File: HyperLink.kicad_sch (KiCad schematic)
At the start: 47 parts, among them J1 USB_C_Receptacle_USB2.0, J2 Conn_02x05_Odd_Even, J3 Conn_02x05_Odd_Even, SW1 SW_Push, U1 ESP32-C3, U2 PESD2USB5UXT, U3 MIC5504-3.3YM5, Y1 ABM11W-40.0000MHZ-8-B1U-T3

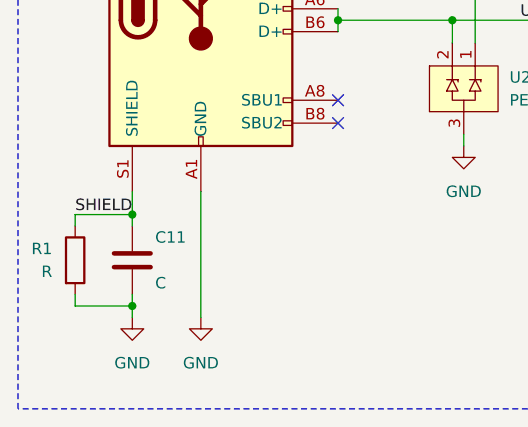
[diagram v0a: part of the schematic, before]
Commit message: Tie SHIELD directly to GND
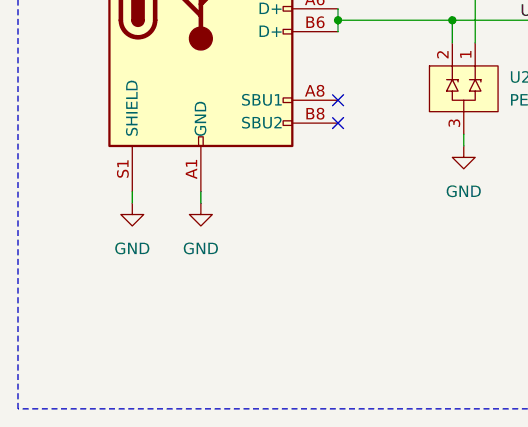
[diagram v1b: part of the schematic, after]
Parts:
- removed C11: C, Capacitor_SMD:C_0402_1005Metric, symbol Device:C
- removed R1: R, Resistor_SMD:R_0402_1005Metric, symbol Device:R
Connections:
- net SHIELD is gone; now on net GND: J1.S1 (SHIELD)
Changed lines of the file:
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@@
   (junction (at 179.07 76.2) (diameter 0) (color 0 0 0 0)
   )
-  (junction (at 29.21 167.64) (diameter 0) (color 0 0 0 0)
-  )
   (junction (at 214.63 139.7) (diameter 0) (color 0 0 0 0)
   )
@@
   )
   (junction (at 250.19 48.26) (diameter 0) (color 0 0 0 0)
-  )
-  (junction (at 29.21 177.8) (diameter 0) (color 0 0 0 0)
   )
   (junction (at 199.39 97.79) (diameter 0) (color 0 0 0 0)
@@
     (stroke (width 0) (type default))
   )
-  (wire (pts (xy 22.86 168.91) (xy 22.86 167.64))
-    (stroke (width 0) (type default))
-  )
   (wire (pts (xy 127 147.32) (xy 119.38 147.32))
     (stroke (width 0) (type default))
@@
     (stroke (width 0) (type default))
   )
-  (wire (pts (xy 29.21 165.1) (xy 29.21 167.64))
-    (stroke (width 0) (type default))
-  )
   (wire (pts (xy 229.87 53.34) (xy 241.3 53.34))
     (stroke (width 0) (type default))
@@
     (stroke (width 0) (type default))
   )
-  (wire (pts (xy 36.83 165.1) (xy 36.83 179.07))
+  (wire (pts (xy 36.83 165.1) (xy 36.83 166.37))
     (stroke (width 0) (type default))
   )
@@
     (stroke (width 0) (type default))
   )
-  (wire (pts (xy 29.21 177.8) (xy 29.21 176.53))
+  (wire (pts (xy 29.21 165.1) (xy 29.21 166.37))
     (stroke (width 0) (type default))
   )
@@
     (stroke (width 0) (type default))
   )
-  (wire (pts (xy 29.21 177.8) (xy 29.21 179.07))
-    (stroke (width 0) (type default))
-  )
   (wire (pts (xy 264.16 48.26) (xy 262.89 48.26))
     (stroke (width 0) (type default))
@@
     (stroke (width 0) (type default))
   )
-  (wire (pts (xy 22.86 177.8) (xy 29.21 177.8))
-    (stroke (width 0) (type default))
-  )
   (wire (pts (xy 243.84 69.85) (xy 252.73 69.85))
     (stroke (width 0) (type default))
@@
     (stroke (width 0) (type default))
   )
-  (wire (pts (xy 22.86 176.53) (xy 22.86 177.8))
-    (stroke (width 0) (type default))
-  )
   (wire (pts (xy 119.38 167.64) (xy 130.81 167.64))
     (stroke (width 0) (type default))
@@
     (stroke (width 0) (type default))
   )
-  (wire (pts (xy 22.86 167.64) (xy 29.21 167.64))
-    (stroke (width 0) (type default))
-  )
   (wire (pts (xy 199.39 100.33) (xy 199.39 97.79))
     (stroke (width 0) (type default))
@@
   )
   (wire (pts (xy 264.16 54.61) (xy 264.16 48.26))
-    (stroke (width 0) (type default))
-  )
-  (wire (pts (xy 29.21 167.64) (xy 29.21 168.91))
     (stroke (width 0) (type default))
   )
@@
   )
   (label "USB_D+" (at 78.74 140.97 180) (fields_autoplaced)
-    (effects (font (size 1.27 1.27)) (justify right bottom))
-  )
-  (label "SHIELD" (at 29.21 167.64 180) (fields_autoplaced)
     (effects (font (size 1.27 1.27)) (justify right bottom))
   )
@@
     )
   )
-  (symbol (lib_id "Device:R") (at 22.86 172.72 0) (unit 1)
-    (in_bom yes) (on_board yes) (dnp no)
-    (property "Reference" "R1" (at 20.32 171.45 0)
-      (effects (font (size 1.27 1.27)) (justify right))
-    )
-    (property "Value" "R" (at 20.32 173.99 0)
-      (effects (font (size 1.27 1.27)) (justify right))
-    )
-    (property "Footprint" "Resistor_SMD:R_0402_1005Metric" (at 21.082 172.72 90)
-      (effects (font (size 1.27 1.27)) hide)
-    )
-    (property "Datasheet" "~" (at 22.86 172.72 0)
-      (effects (font (size 1.27 1.27)) hide)
-    )
-    (pin "1")
-    (pin "2")
-    (instances
-      (project "HyperLink"
-        (path "/0c11886f-ef87-4398-b8dc-47aef68c9619"
-          (reference "R1") (unit 1)
-        )
-      )
-    )
-  )
   (symbol (lib_id "power:GND") (at 105.41 154.94 270) (unit 1)
     (in_bom yes) (on_board yes) (dnp no)
@@
         (path "/0c11886f-ef87-4398-b8dc-47aef68c9619"
           (reference "C3") (unit 1)
-        )
-      )
-    )
-  )
-  (symbol (lib_id "Device:C") (at 29.21 172.72 0) (unit 1)
-    (in_bom yes) (on_board yes) (dnp no)
-    (property "Reference" "C11" (at 31.75 170.18 0)
-      (effects (font (size 1.27 1.27)) (justify left))
-    )
-    (property "Value" "C" (at 31.75 175.26 0)
-      (effects (font (size 1.27 1.27)) (justify left))
-    )
-    (property "Footprint" "Capacitor_SMD:C_0402_1005Metric" (at 30.1752 176.53 0)
-      (effects (font (size 1.27 1.27)) hide)
-    )
-    (property "Datasheet" "~" (at 29.21 172.72 0)
-      (effects (font (size 1.27 1.27)) hide)
-    )
-    (pin "1")
-    (pin "2")
-    (instances
-      (project "HyperLink"
-        (path "/0c11886f-ef87-4398-b8dc-47aef68c9619"
-          (reference "C11") (unit 1)
         )
       )
@@
     )
   )
-  (symbol (lib_id "power:GND") (at 29.21 179.07 0) (unit 1)
-    (in_bom yes) (on_board yes) (dnp no) (fields_autoplaced)
-    (property "Reference" "#PWR013" (at 29.21 185.42 0)
-      (effects (font (size 1.27 1.27)) hide)
-    )
-    (property "Value" "GND" (at 29.21 184.15 0)
-      (effects (font (size 1.27 1.27)))
-    )
-    (property "Footprint" "" (at 29.21 179.07 0)
-      (effects (font (size 1.27 1.27)) hide)
-    )
-    (property "Datasheet" "" (at 29.21 179.07 0)
+  (symbol (lib_id "power:GND") (at 29.21 166.37 0) (unit 1)
+    (in_bom yes) (on_board yes) (dnp no) (fields_autoplaced)
+    (property "Reference" "#PWR013" (at 29.21 172.72 0)
+      (effects (font (size 1.27 1.27)) hide)
+    )
+    (property "Value" "GND" (at 29.21 171.45 0)
+      (effects (font (size 1.27 1.27)))
+    )
+    (property "Footprint" "" (at 29.21 166.37 0)
+      (effects (font (size 1.27 1.27)) hide)
+    )
+    (property "Datasheet" "" (at 29.21 166.37 0)
       (effects (font (size 1.27 1.27)) hide)
     )
@@
     )
   )
-  (symbol (lib_id "power:GND") (at 36.83 179.07 0) (unit 1)
-    (in_bom yes) (on_board yes) (dnp no)
-    (property "Reference" "#PWR012" (at 36.83 185.42 0)
-      (effects (font (size 1.27 1.27)) hide)
-    )
-    (property "Value" "GND" (at 36.83 184.15 0)
-      (effects (font (size 1.27 1.27)))
-    )
-    (property "Footprint" "" (at 36.83 179.07 0)
-      (effects (font (size 1.27 1.27)) hide)
-    )
-    (property "Datasheet" "" (at 36.83 179.07 0)
-      (effects (font (size 1.27 1.27)) hide)
-    )
+  (symbol (lib_id "power:GND") (at 36.83 166.37 0) (unit 1)
+    (in_bom yes) (on_board yes) (dnp no)
+    (property "Reference" "#PWR012" (at 36.83 172.72 0)
+      (effects (font (size 1.27 1.27)) hide)
+    )
+    (property "Value" "GND" (at 36.83 171.45 0)
+      (effects (font (size 1.27 1.27)))
+    )
+    (property "Footprint" "" (at 36.83 166.37 0)
+      (effects (font (size 1.27 1.27)) hide)
+    )
+    (property "Datasheet" "" (at 36.83 166.37 0)
+      (effects (font (size 1.27 1.27)) hide)
+    )

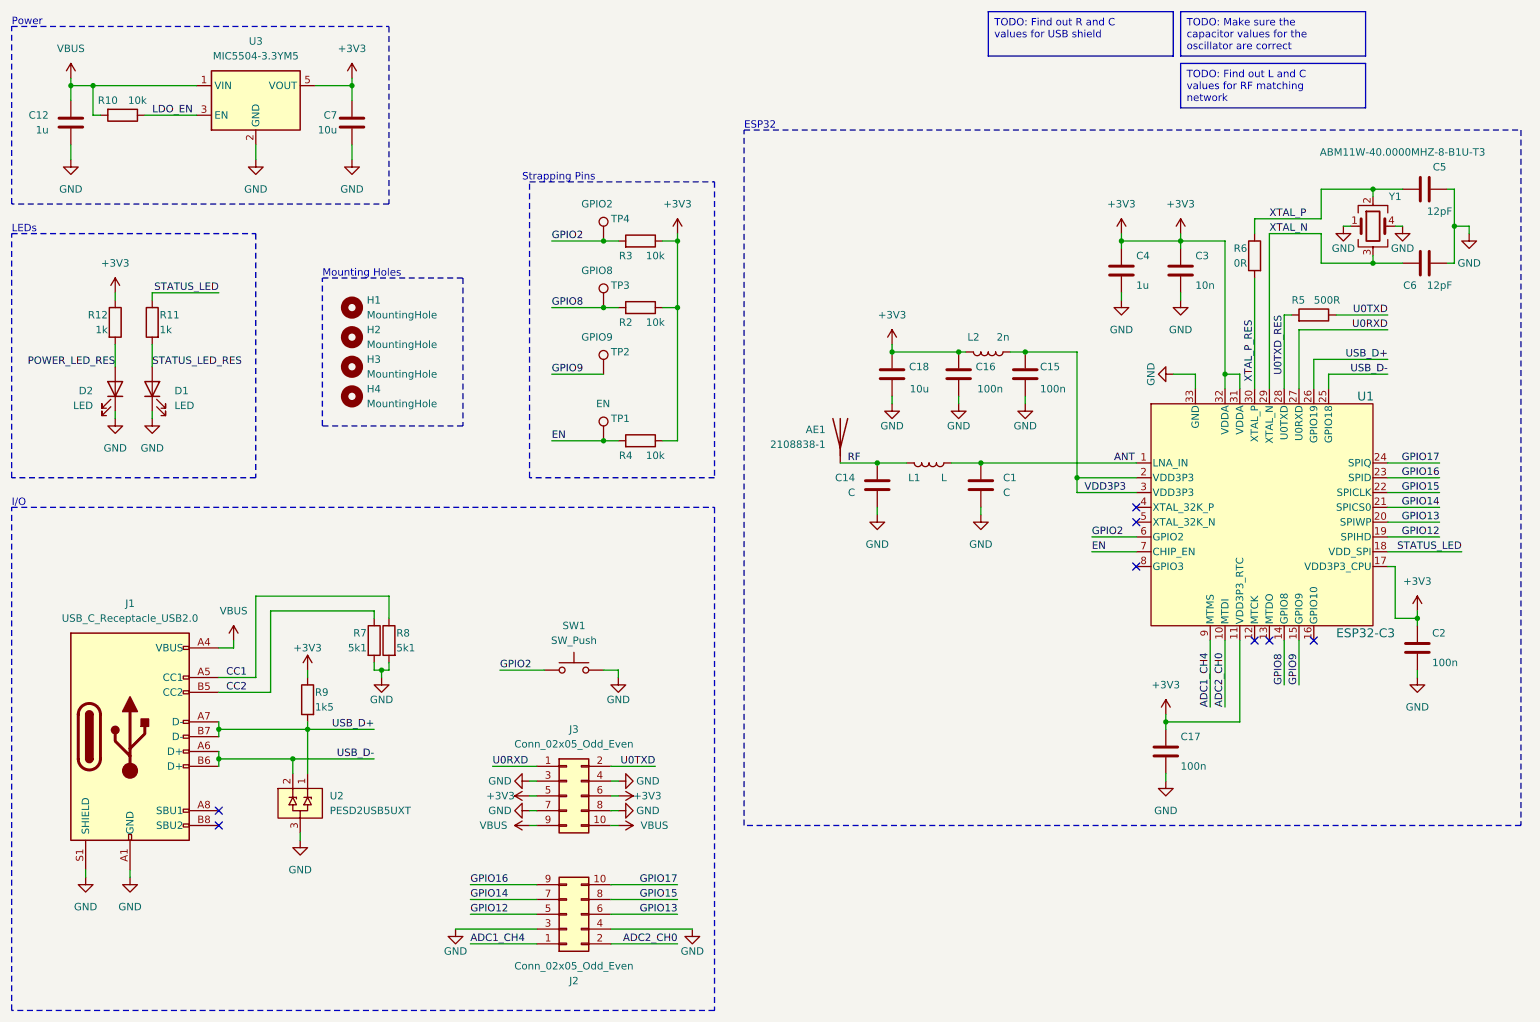
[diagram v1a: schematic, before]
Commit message: Fix last remaining TODOs and clean up schematic
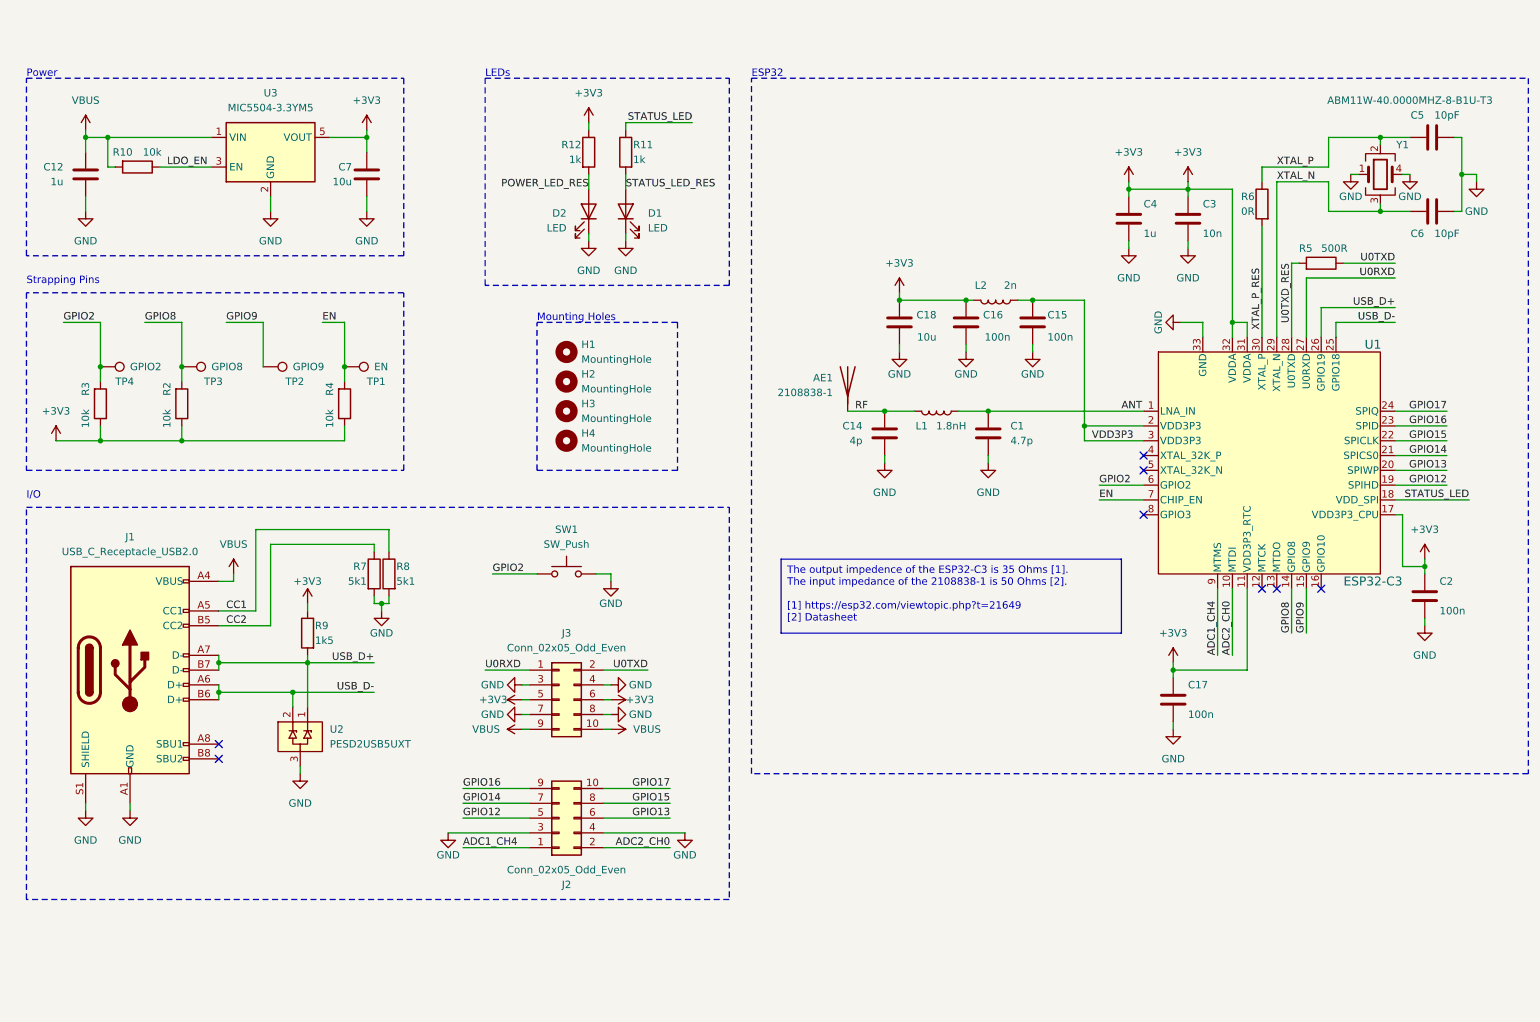
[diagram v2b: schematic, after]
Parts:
- C1: value C -> 4.7p
- C14: value C -> 4p
- C5, C6: value 12pF -> 10pF
- L1: value L -> 1.8nH
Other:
- moved on the sheet: AE1, C1, C12, C14, C15, C16, C17, C18, C2, C3, C4, C5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

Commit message: Replace Antenna symbol with chip antenna
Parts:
- removed AE1: 2108838-1, encyclopedia_galactica:2108838-1, symbol Device:Antenna
- added AE1: 2108838-1, encyclopedia_galactica:2108838-1, symbol Device:Antenna_Chip
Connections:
- net RF: now also AE1.1 (FEED)
- no-connect marks 8 -> 9
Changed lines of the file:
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@@
   (no_connect (at 233.68 116.84))
   (no_connect (at 210.82 96.52))
+  (no_connect (at 154.94 86.36))
   (wire (pts (xy 52.07 133.35) (xy 52.07 134.62))
     (stroke (width 0) (type default))
@@
     )
   )
-  (symbol (lib_id "Device:Antenna") (at 160.02 81.28 0) (mirror y) (unit 1)
-    (in_bom yes) (on_board yes) (dnp no)
-    (property "Reference" "AE1" (at 157.48 80.645 0)
-      (effects (font (size 1.27 1.27)) (justify left))
-    )
-    (property "Value" "2108838-1" (at 157.48 83.185 0)
-      (effects (font (size 1.27 1.27)) (justify left))
-    )
-    (property "Footprint" "encyclopedia_galactica:2108838-1" (at 160.02 81.28 0)
-      (effects (font (size 1.27 1.27)) hide)
-    )
-    (property "Datasheet" "https://www.te.com/commerce/DocumentDelivery/DDEController?Action=showdoc&DocId=Data+Sheet%7F2108838%7FA2%7Fpdf%7FEnglish%7FENG_DS_2108838_A2.pdf%7F2108838-1" (at 160.02 81.28 0)
-      (effects (font (size 1.27 1.27)) hide)
-    )
-    (pin "1")
-    (instances
-      (project "HyperLink"
-        (path "/0c11886f-ef87-4398-b8dc-47aef68c9619"
-          (reference "AE1") (unit 1)
-        )
-      )
-    )
-  )
   (symbol (lib_id "Mechanical:MountingHole") (at 111.76 81.28 0) (unit 1)
     (in_bom yes) (on_board yes) (dnp no) (fields_autoplaced)
@@
         )
       )
+    )
+  )
+  (symbol (lib_id "Device:Antenna_Chip") (at 157.48 83.82 0) (mirror y) (unit 1)
+    (in_bom yes) (on_board yes) (dnp no)
+    (property "Reference" "AE1" (at 149.86 82.55 0)
+      (effects (font (size 1.27 1.27)) (justify right))
+    )
+    (property "Value" "2108838-1" (at 149.86 74.93 0)
+      (effects (font (size 1.27 1.27)) (justify right))
+    )
+    (property "Footprint" "encyclopedia_galactica:2108838-1" (at 160.02 79.375 0)
+      (effects (font (size 1.27 1.27)) hide)
+    )
+    (property "Datasheet" "https://www.te.com/commerce/DocumentDelivery/DDEController?Action=showdoc&DocId=Data+Sheet%7F2108838%7FA2%7Fpdf%7FEnglish%7FENG_DS_2108838_A2.pdf%7F2108838-1" (at 160.02 79.375 0)
+      (effects (font (size 1.27 1.27)) hide)
+    )
+    (pin "1")
+    (pin "2")
+    (instances
+      (project "HyperLink"
+        (path "/0c11886f-ef87-4398-b8dc-47aef68c9619"
+          (reference "AE1") (unit 1)
+        )
+      )

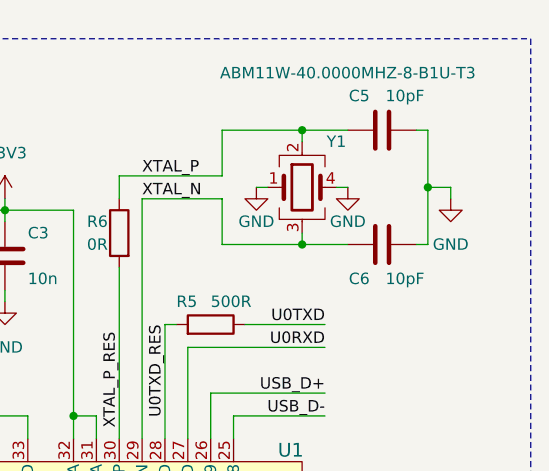
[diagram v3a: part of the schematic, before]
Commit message: Remove 'F' from capacitor values
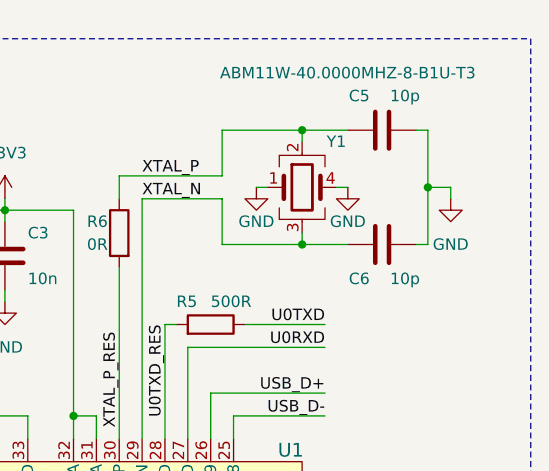
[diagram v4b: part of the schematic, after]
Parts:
- C5, C6: value 10pF -> 10p
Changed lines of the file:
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@@
       (effects (font (size 1.27 1.27)))
     )
-    (property "Value" "10pF" (at 262.89 55.88 90)
+    (property "Value" "10p" (at 262.89 55.88 90)
       (effects (font (size 1.27 1.27)))
     )
@@
       (effects (font (size 1.27 1.27)))
     )
-    (property "Value" "10pF" (at 262.89 35.56 90)
-      (effects (font (size 1.27 1.27)))
-    )
+    (property "Value" "10p" (at 262.89 35.56 90)
+      (effects (font (size 1.27 1.27)))
+    )

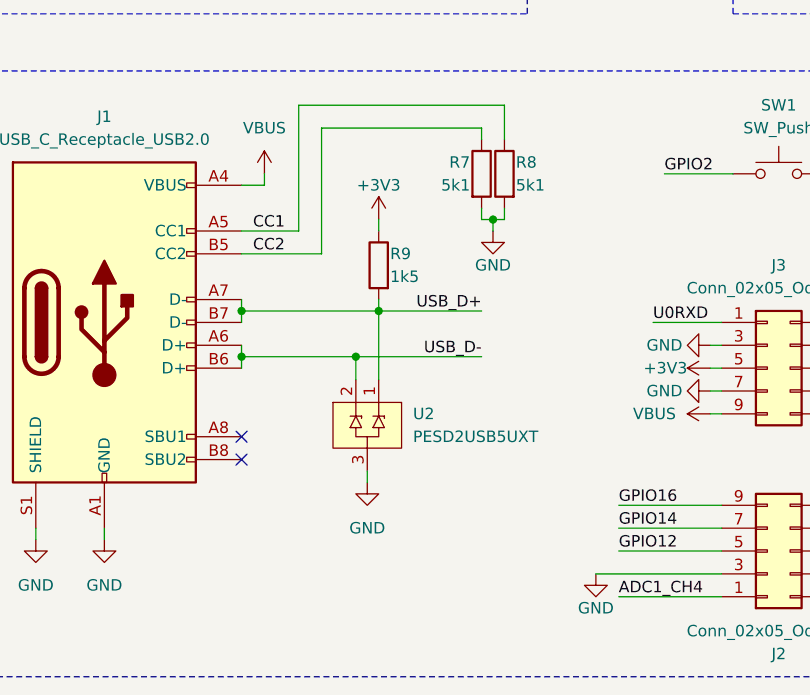
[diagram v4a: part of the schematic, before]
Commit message: Flip D+ and D- at connector
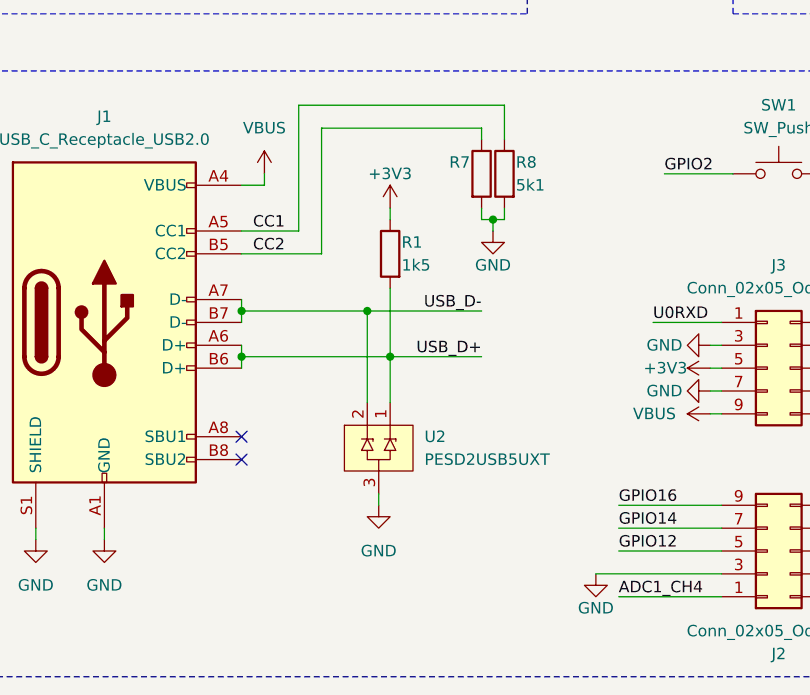
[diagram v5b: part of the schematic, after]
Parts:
- removed R9: 1k5, Resistor_SMD:R_0402_1005Metric, symbol Device:R
- added R1: 1k5, Resistor_SMD:R_0402_1005Metric, symbol Device:R
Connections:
- net +3V3: now also R1.1
- net USB_D+: now also J1.A6 (D+), J1.B6 (D+), R1.2; no longer J1.A7 (D-), J1.B7 (D-)
- net USB_D-: now also J1.A7 (D-), J1.B7 (D-); no longer J1.A6 (D+), J1.B6 (D+)
